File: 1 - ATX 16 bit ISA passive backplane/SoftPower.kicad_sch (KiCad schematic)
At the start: 65 parts, among them J10 ATX POWER, J11 PWR IN SEL, J12 PWR SW SEL, J19 3V/-5V, U1 74HCT14, U3 74HCT74, U4 LM7905

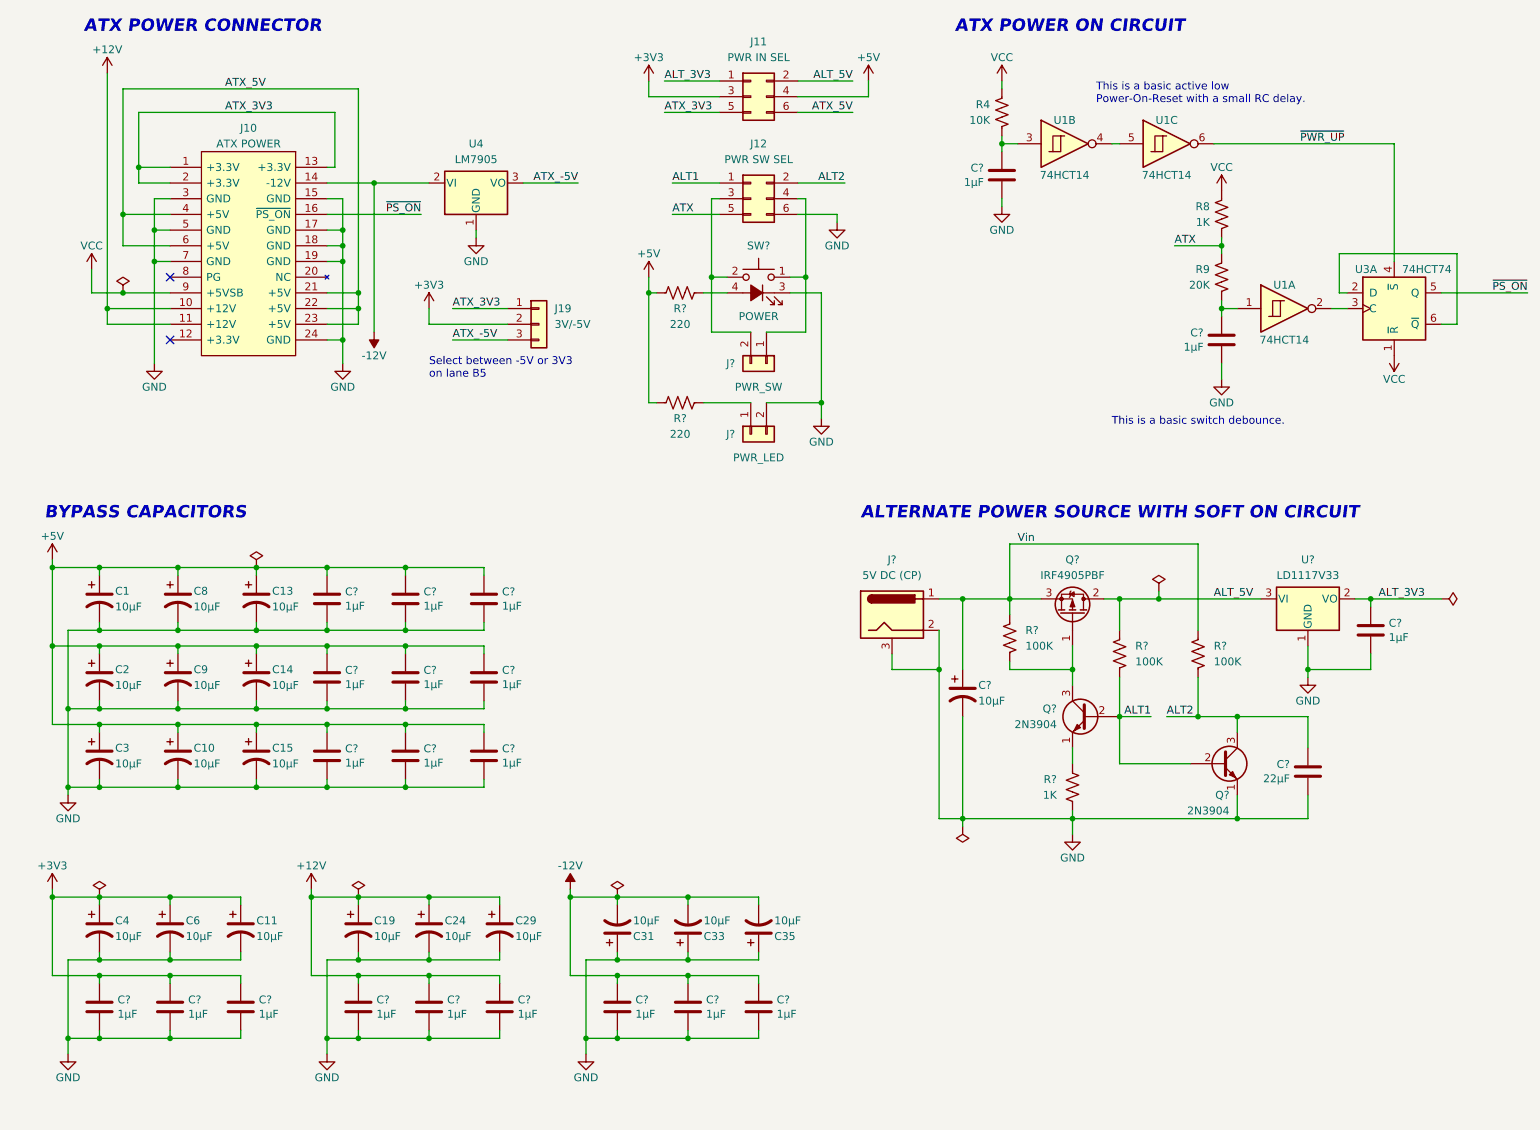
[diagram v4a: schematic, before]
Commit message: Removed the alternate power input.
The soft power on circuit was flaky upon testing.
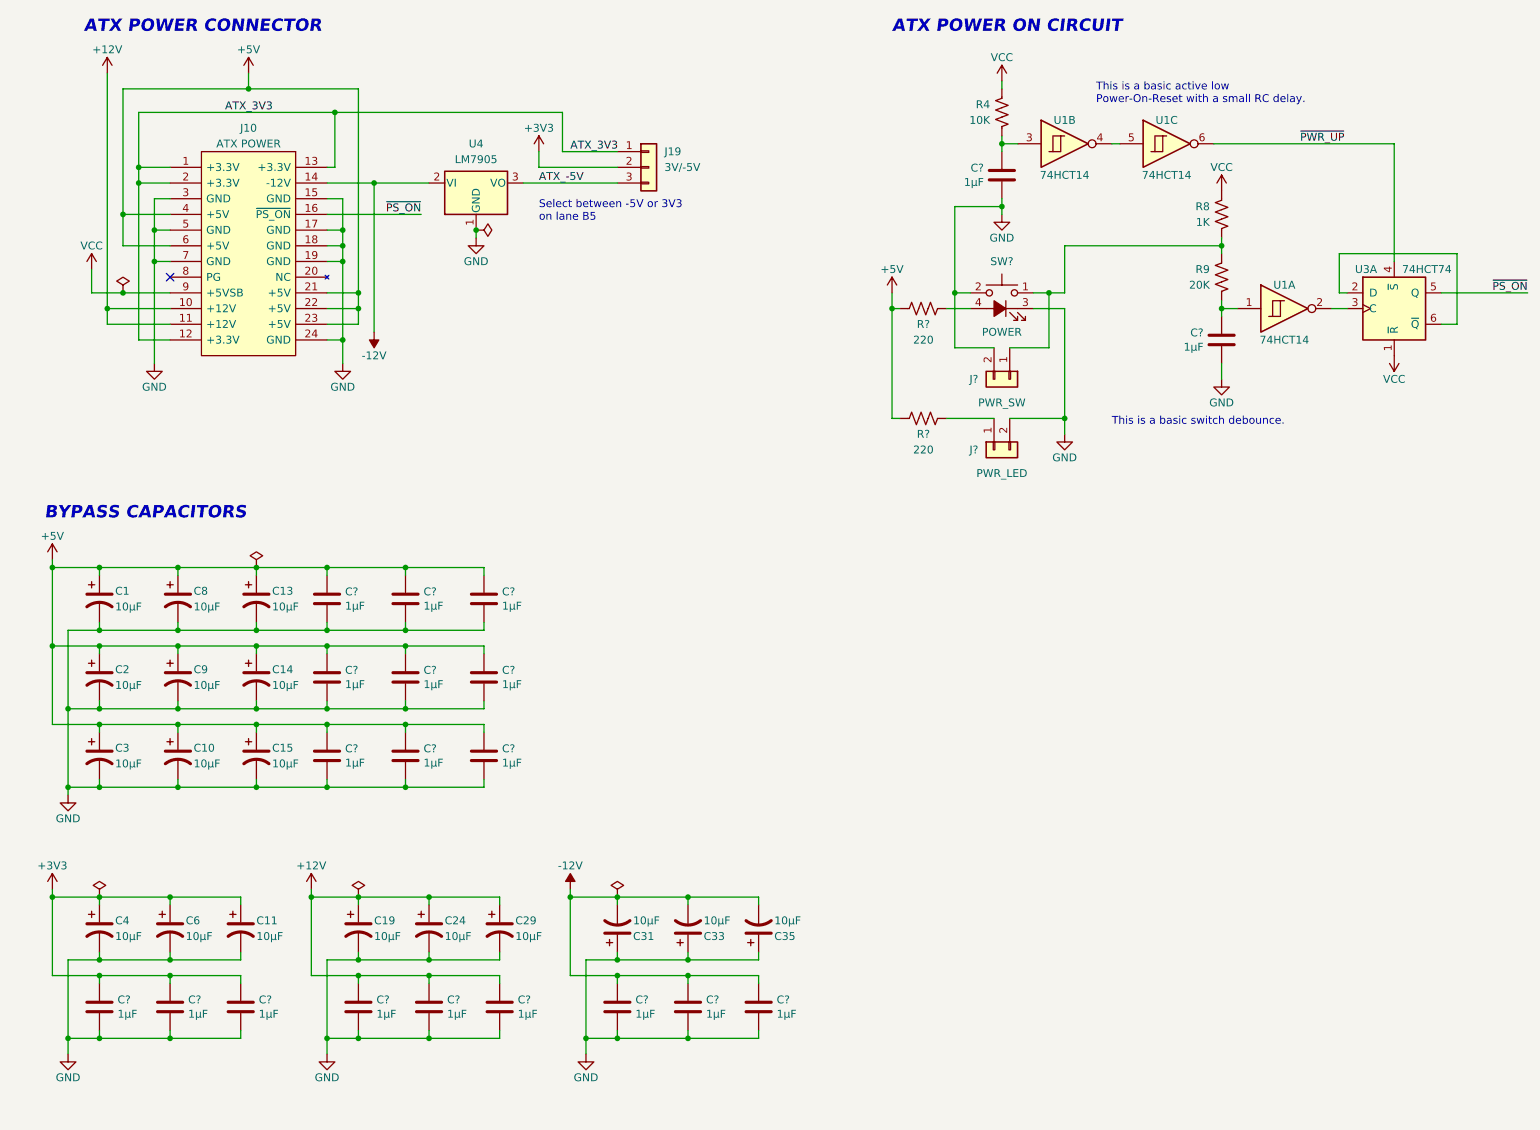
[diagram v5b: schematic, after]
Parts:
- removed C?: 10µF, Capacitor_THT:CP_Radial_D6.3mm_P2.50mm, symbol Device:C_Polarized_US
- removed C?: 22µF, Capacitor_THT:C_Disc_D3.0mm_W1.6mm_P2.50mm, symbol Device:C
- removed C?: 1µF, Capacitor_THT:C_Disc_D3.0mm_W1.6mm_P2.50mm, symbol Device:C
- removed J11: PWR IN SEL, Connector_PinHeader_2.54mm:PinHeader_2x03_P2.54mm_Vertical, symbol Connector_Generic:Conn_02x03_Odd_Even
- removed J12: PWR SW SEL, Connector_PinHeader_2.54mm:PinHeader_2x03_P2.54mm_Vertical, symbol Connector_Generic:Conn_02x03_Odd_Even
- removed J?: 5V DC (CP), Connector_BarrelJack:BarrelJack_Horizontal, symbol 0_Library:Barrel_Jack
- removed Q? (x2): 2N3904, Package_TO_SOT_THT:TO-92_Inline_Wide, symbol Transistor_BJT:2N3904
- removed Q?: IRF4905PBF, Package_TO_SOT_THT:TO-220-3_Horizontal_TabDown, symbol Transistor_FET:IRF4905
- removed R?: 1K, Resistor_THT:R_Axial_DIN0207_L6.3mm_D2.5mm_P10.16mm_Horizontal, symbol Device:R_US
- removed R? (x3): 100K, Resistor_THT:R_Axial_DIN0207_L6.3mm_D2.5mm_P10.16mm_Horizontal, symbol Device:R_US
- removed U?: LD1117V33, Package_TO_SOT_THT:TO-220-3_Horizontal_TabDown, symbol 0_Library:LM1117-3.3
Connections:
- net ATX is gone; now on an unnamed net: R8.2, R9.1
- net ATX_5V is gone; now on net +5V: J10.21 (+5V), J10.22 (+5V), J10.23 (+5V), J10.4 (+5V), J10.6 (+5V)
- net ATX_3V3: now also J10.12 (+3.3V)
- net GND: now also J?.2 (Pin_2), SW?.2
- no-connect marks 2 -> 1
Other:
- note removed: "ALTERNATE POWER SOURCE WITH SOFT ON CIRCUIT"
- moved on the sheet: J19, J?, R?, SW?
